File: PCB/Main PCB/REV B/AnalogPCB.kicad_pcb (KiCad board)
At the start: 4 copper layers, 60 x 100 mm, 75 parts, among them J1 DF12NB_4.0_-20DP-0.5V_51_, J2 393570002, J3 393570002, J4 393570002, J5 393570002, J6 SJ3-35053D, Q1 2N7002, Q2 2N7002, Q3 2N7002, U1 ALDP105W, U2 ALDP105W, U3 ALDP105W

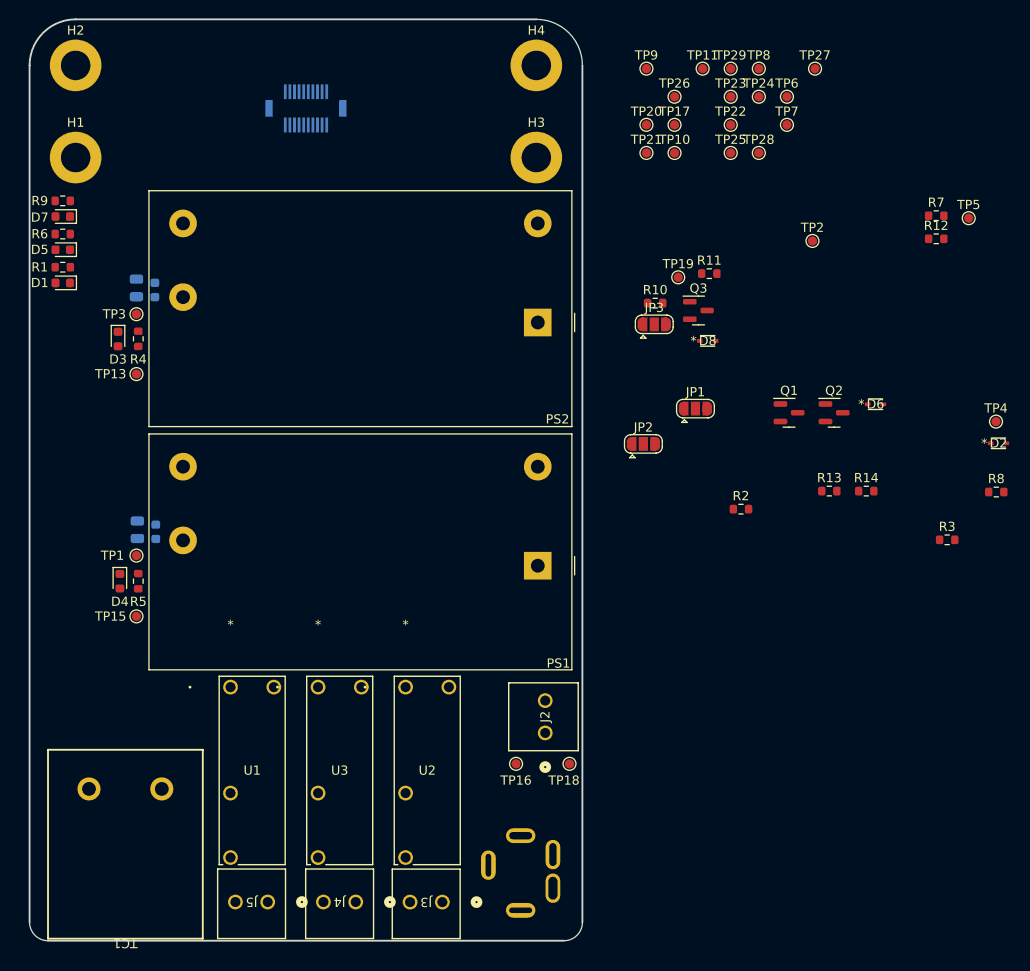
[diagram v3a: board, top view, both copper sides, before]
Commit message: PCB - Lay out analog mostly complete. cad added
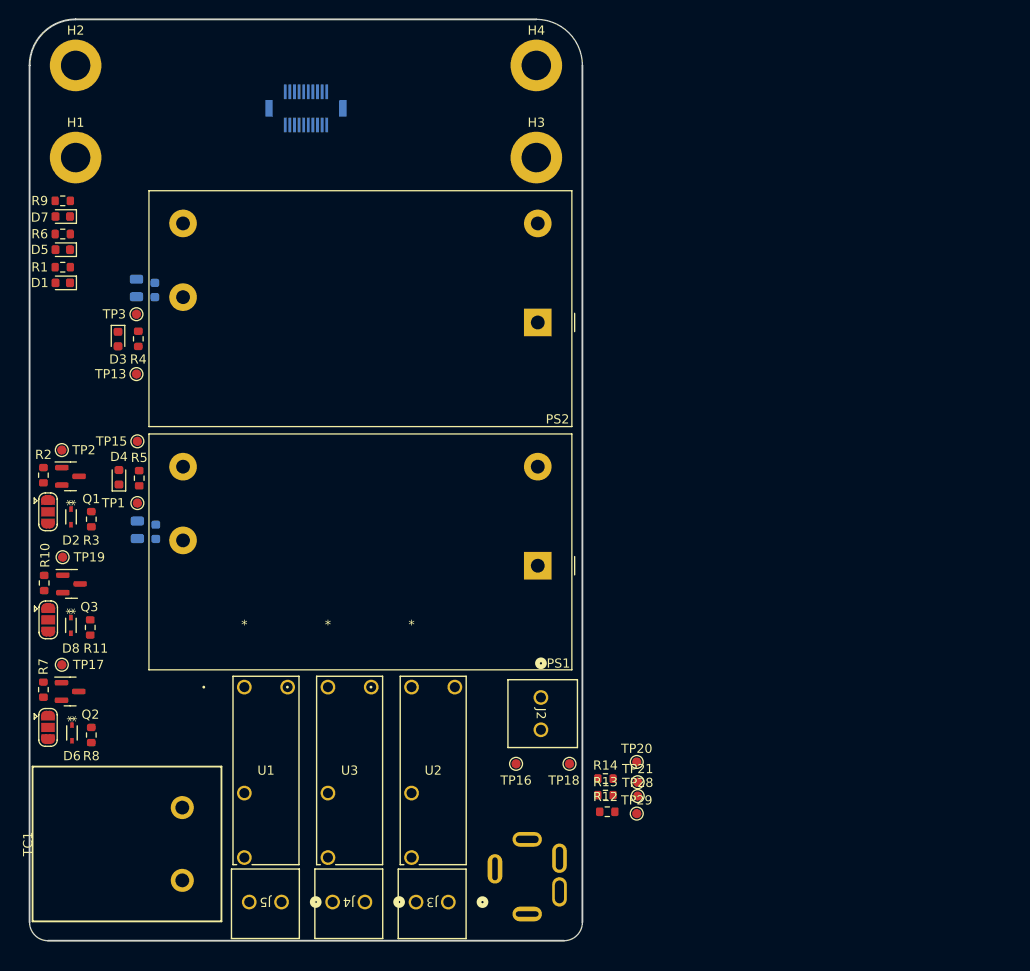
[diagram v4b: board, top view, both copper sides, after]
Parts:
- removed TP10, TP11, TP22, TP23, TP24, TP25, TP26, TP27, TP4, TP5, TP6, TP7, TP8, TP9: TP, TestPoint:TestPoint_Pad_D1.0mm
- moved R7 109.7 mm to (51.5, 122.7), turned to 90 degrees
- moved R8 101.7 mm to (56.7, 127.7), turned to 90 degrees
- moved D2 101.0 mm to (54.5, 104.0), turned to -90 degrees
- moved D6 94.2 mm to (54.6, 127.4), turned to -90 degrees
- moved R3 92.9 mm to (56.7, 104.2), turned to 90 degrees
- moved TP17 88.6 mm to (53.5, 120.0)
- moved Q2 88.3 mm to (54.4, 122.9)
- moved TP2 84.6 mm to (53.5, 96.7), turned to 90 degrees
- moved TP29 81.5 mm to (115.9, 136.2)
- moved Q1 78.3 mm to (54.4, 99.6)
- moved R11 77.4 mm to (56.6, 116.0), turned to 90 degrees
- moved R2 75.8 mm to (51.5, 99.5), turned to 90 degrees
- moved D8 75.7 mm to (54.5, 115.8), turned to -90 degrees
- moved Q3 74.2 mm to (54.5, 111.3)
- moved TP19 73.4 mm to (53.6, 108.4)
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
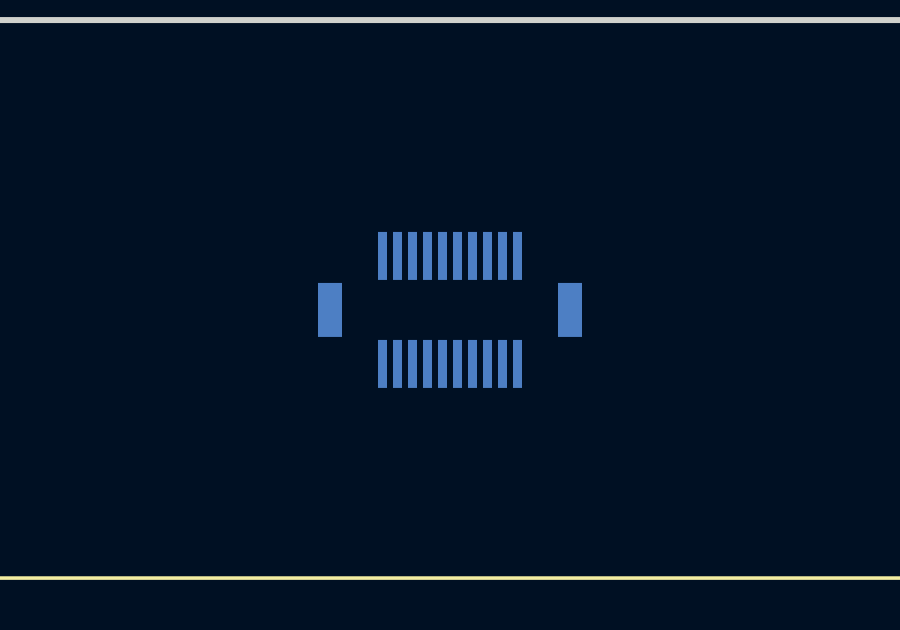
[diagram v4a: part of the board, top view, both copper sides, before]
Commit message: PCB - Grouping for digital layout
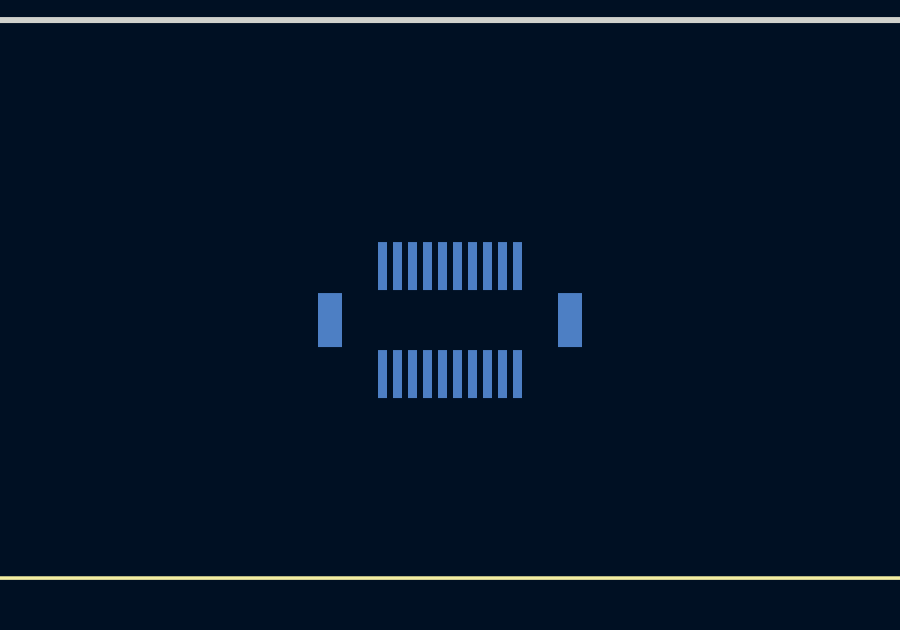
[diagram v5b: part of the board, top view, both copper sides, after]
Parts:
- moved J1 0.34 mm to (80.0, 60.0)
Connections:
- J1 pad 18: /MeatProbeSleeve -> GND
- J1 pad 19: /MeatProbeRing -> /MeatProbe+
- J1 pad 20: /MeatProbeTip -> /MeatProbe-
- J6 pad 1: /MeatProbeSleeve -> /MeatProbe-
- J6 pad 3: /MeatProbeRing -> GND

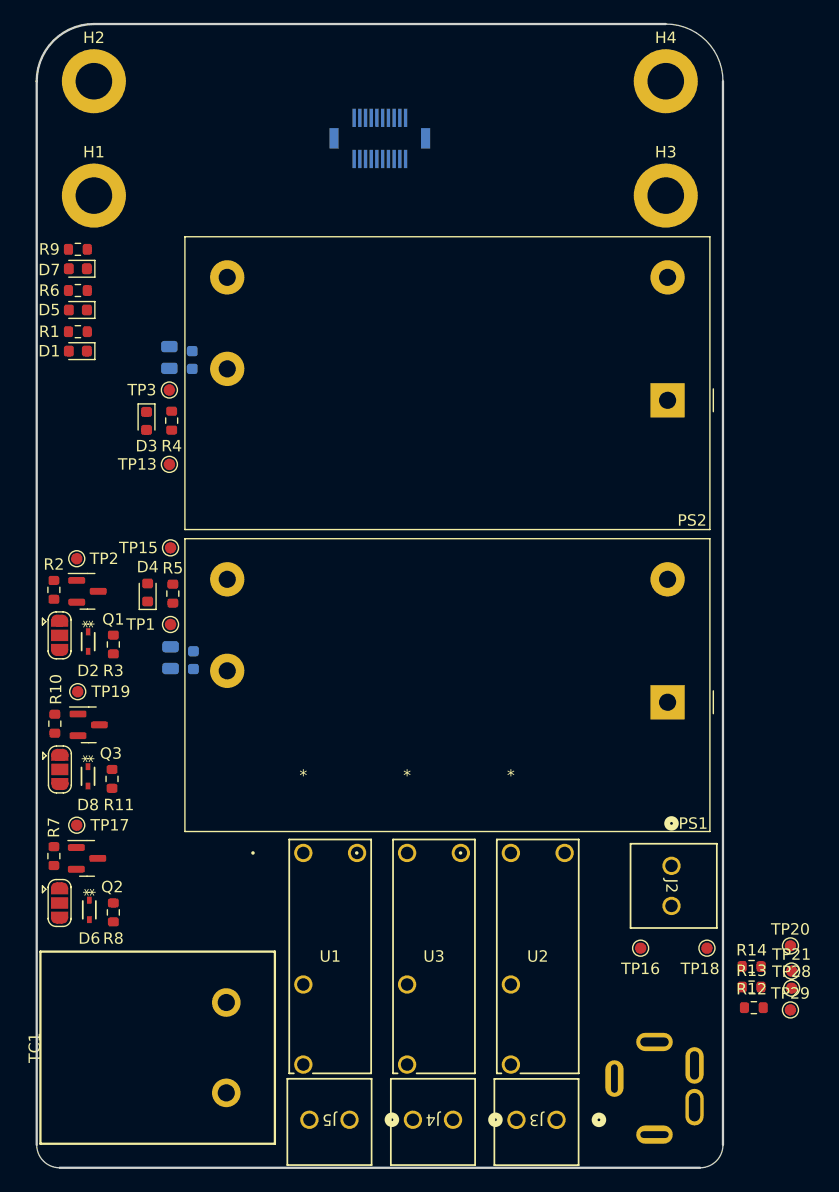
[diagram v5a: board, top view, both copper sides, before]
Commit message: PCB - Digital/analog layout complete - ready to review
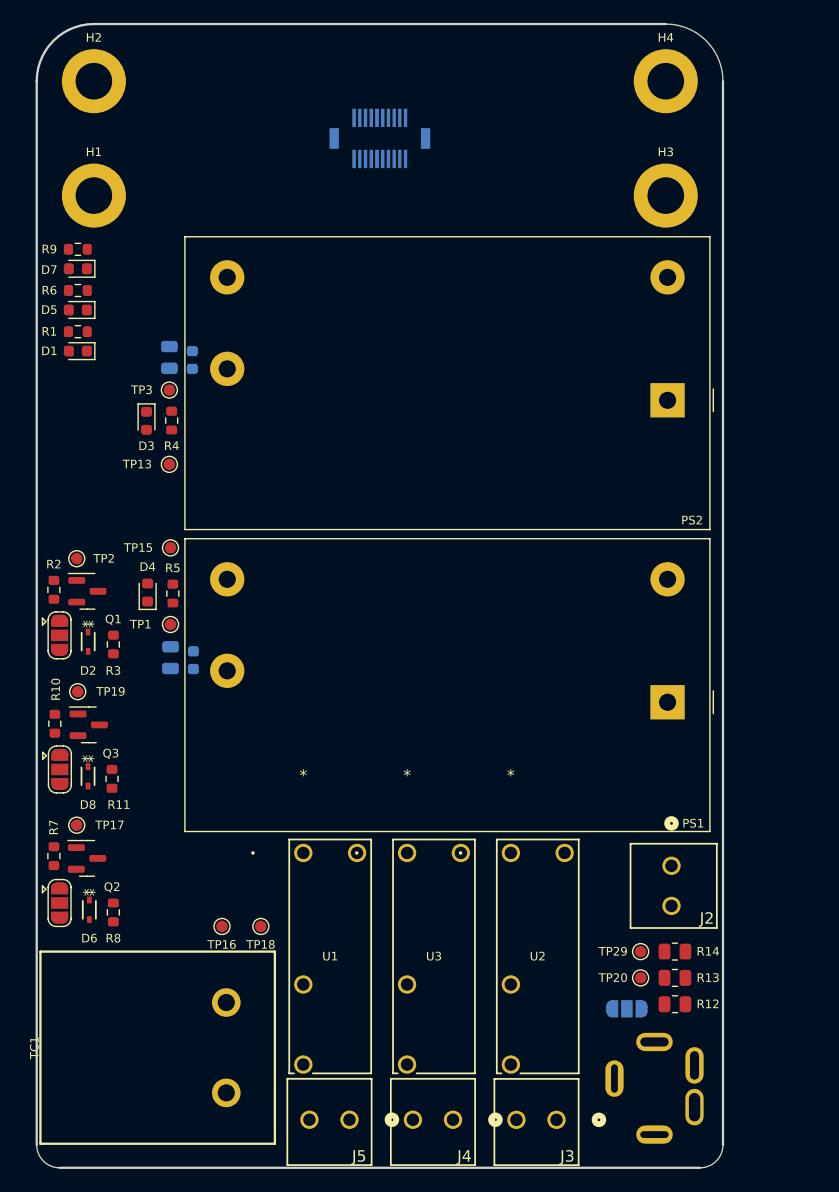
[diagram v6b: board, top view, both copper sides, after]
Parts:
- removed TP21, TP28: TP, TestPoint:TestPoint_Pad_D1.0mm
- added JP4: SolderJumper_3_Open, Jumper:SolderJumper-3_P1.3mm_Open_RoundedPad1.0x1.5mm, B.Cu at (101.6, 136.1)
- R12, R13, R14: value 1kOhm 1% 0603 -> 1kOhm 0.1% 0805; footprint Resistor_SMD:R_0603_1608Metric -> Resistor_SMD:R_0805_2012Metric
- moved TP18 39.0 mm to (69.6, 128.9)
- moved TP16 36.6 mm to (66.2, 128.9)
- moved TP29 14.1 mm to (102.8, 131.1)
- moved TP20 13.4 mm to (102.8, 133.4)
- moved R12 6.91 mm to (105.8, 135.7)
- moved R14 6.82 mm to (105.8, 131.1), turned to 180 degrees
- moved R13 6.75 mm to (105.8, 133.4)
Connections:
- J6 pad 1: /MeatProbe- -> /MeatProbeSleeve
- J6 pad 3: GND -> /MeatProbe-

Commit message: PCB - Analog Routing Begin
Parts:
- moved R12 53.9 mm to (52.7, 144.8)
- moved R13 53.9 mm to (52.7, 142.5)
- moved R14 53.9 mm to (52.7, 140.2)
- moved TP29 53.4 mm to (52.0, 147.4), turned to 90 degrees
- moved TP20 49.7 mm to (55.1, 147.4), turned to 90 degrees
- moved TP16 41.5 mm to (107.6, 131.4), turned to -90 degrees
- moved J6 39.2 mm to (61.7, 147.6), turned to -90 degrees
- moved JP4 38.9 mm to (62.7, 137.8)
- moved TP18 34.7 mm to (104.2, 131.4), turned to -90 degrees
- moved J2 12.8 mm to (105.6, 136.4)
- moved TC1 9.30 mm to (50.3, 130.2)
- moved D2 9.07 mm to (54.5, 94.9)
- moved D6 9.07 mm to (54.6, 118.4)
- moved D8 9.07 mm to (54.5, 106.7)
- moved JP1 9.07 mm to (52.0, 94.4)
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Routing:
- net /Opto_Auger: track 0.00 -> 3.90 mm
- net Net-(D5-Pad2): track 0.00 -> 1.72 mm
- net Net-(D7-Pad2): track 0.00 -> 1.72 mm
- net Net-(D1-Pad2): track 0.00 -> 1.72 mm
- added copper zone on B.Cu, net GND
- added copper zone on F.Cu, net GND
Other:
- copper layers 4 -> 2
